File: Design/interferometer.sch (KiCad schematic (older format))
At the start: 30 parts, among them Q1 FDC637BNZ, U1 ADN8810ACPZ, U2 OPA320SAIDBVT, U3 ADR292GRUZ

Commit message: Modify schematic
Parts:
- added R? (x4): 100k, symbol R
- R3: value R -> 66.5R
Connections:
- net 3v3: now also R?.1, R?.1, R?.1, R?.1
- net ~CS: now also R?.2
- net ~SHDN: now also R?.2
- net ~laser_reset: now also R?.2
- net ~laser_standby: now also R?.2
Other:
- moved on the sheet: C10, C9, TP4
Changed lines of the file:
@@
 Text Label 6550 1700 0    60   ~ 0
 SCK
-Text Label 6550 2000 0    60   ~ 0
+Text Label 7050 2000 0    60   ~ 0
 ~CS
 Text Label 4050 2600 0    60   ~ 0
@@
 Text Label 6550 1600 0    60   ~ 0
 GND
-Text Label 2700 3600 1    60   ~ 0
+Text Label 2450 3900 1    60   ~ 0
 GND
 $Comp
 L GNDA #PWR01
 U 1 1 591C35DD
-P 2500 4050
-F 0 "#PWR01" H 2500 3800 50  0001 C CNN
-F 1 "GNDA" H 2505 3877 50  0000 C CNN
-F 2 "" H 2500 4050 50  0001 C CNN
-F 3 "" H 2500 4050 50  0001 C CNN
-	1    2500 4050
+P 2250 4350
+F 0 "#PWR01" H 2250 4100 50  0001 C CNN
+F 1 "GNDA" H 2255 4177 50  0000 C CNN
+F 2 "" H 2250 4350 50  0001 C CNN
+F 3 "" H 2250 4350 50  0001 C CNN
+	1    2250 4350
 	1    0    0    -1
 $EndComp
@@
 L Earth #PWR02
 U 1 1 591C415F
-P 2900 4050
-F 0 "#PWR02" H 2900 3800 50  0001 C CNN
-F 1 "Earth" H 2900 3900 50  0001 C CNN
-F 2 "" H 2900 4050 50  0001 C CNN
-F 3 "" H 2900 4050 50  0001 C CNN
-	1    2900 4050
+P 2650 4350
+F 0 "#PWR02" H 2650 4100 50  0001 C CNN
+F 1 "Earth" H 2650 4200 50  0001 C CNN
+F 2 "" H 2650 4350 50  0001 C CNN
+F 3 "" H 2650 4350 50  0001 C CNN
+	1    2650 4350
 	1    0    0    -1
 $EndComp
@@
 Text Label 7300 1450 0    60   ~ 0
 4.096_VREF
-Text Label 7450 1550 0    60   ~ 0
+Text Label 7400 1550 0    60   ~ 0
 ~laser_reset
-Text Label 8050 3000 0    60   ~ 0
+Text Label 8050 3000 2    60   ~ 0
 ~laser_standby
 NoConn ~ 10000 1400
@@
 L C C9
 U 1 1 591CDD86
-P 1050 5250
-F 0 "C9" H 1150 5250 50  0000 L CNN
-F 1 "22uF" H 1100 5150 50  0000 L CNN
-F 2 "" H 1088 5100 50  0001 C CNN
-F 3 "" H 1050 5250 50  0001 C CNN
-	1    1050 5250
+P 1050 5550
+F 0 "C9" H 1150 5550 50  0000 L CNN
+F 1 "22uF" H 1100 5450 50  0000 L CNN
+F 2 "" H 1088 5400 50  0001 C CNN
+F 3 "" H 1050 5550 50  0001 C CNN
+	1    1050 5550
 	1    0    0    -1
 $EndComp
@@
 L GNDA #PWR010
 U 1 1 591CE000
-P 1050 5500
-F 0 "#PWR010" H 1050 5250 50  0001 C CNN
-F 1 "GNDA" H 1055 5327 50  0000 C CNN
-F 2 "" H 1050 5500 50  0001 C CNN
-F 3 "" H 1050 5500 50  0001 C CNN
-	1    1050 5500
+P 1050 5800
+F 0 "#PWR010" H 1050 5550 50  0001 C CNN
+F 1 "GNDA" H 1055 5627 50  0000 C CNN
+F 2 "" H 1050 5800 50  0001 C CNN
+F 3 "" H 1050 5800 50  0001 C CNN
+	1    1050 5800
 	1    0    0    -1
 $EndComp
@@
 U 1 1 591CE293
 P 7230 4820
-F 0 "R3" H 7300 4866 50  0000 L CNN
-F 1 "R" H 7300 4775 50  0000 L CNN
+F 0 "R3" H 7000 4890 50  0000 L CNN
+F 1 "66.5R" H 6950 4790 50  0000 L CNN
 F 2 "Resistors_SMD:R_0805" V 7160 4820 50  0001 C CNN
 F 3 "" H 7230 4820 50  0001 C CNN
@@
 Text Label 5700 6300 2    60   ~ 0
 AVSS
-Text Label 800  5000 0    60   ~ 0
+Text Label 800  5300 0    60   ~ 0
 3v3
 $Comp
 L C C10
 U 1 1 591D633E
-P 2450 5250
-F 0 "C10" H 2550 5250 50  0000 L CNN
-F 1 "22uF" H 2500 5150 50  0000 L CNN
-F 2 "" H 2488 5100 50  0001 C CNN
-F 3 "" H 2450 5250 50  0001 C CNN
-	1    2450 5250
+P 2450 5550
+F 0 "C10" H 2550 5550 50  0000 L CNN
+F 1 "22uF" H 2500 5450 50  0000 L CNN
+F 2 "" H 2488 5400 50  0001 C CNN
+F 3 "" H 2450 5550 50  0001 C CNN
+	1    2450 5550
 	1    0    0    -1
 $EndComp
@@
 L GNDA #PWR011
 U 1 1 591D6345
-P 2450 5500
-F 0 "#PWR011" H 2450 5250 50  0001 C CNN
-F 1 "GNDA" H 2455 5327 50  0000 C CNN
-F 2 "" H 2450 5500 50  0001 C CNN
-F 3 "" H 2450 5500 50  0001 C CNN
-	1    2450 5500
-	1    0    0    -1
-$EndComp
-Text Label 2200 5000 0    60   ~ 0
+P 2450 5800
+F 0 "#PWR011" H 2450 5550 50  0001 C CNN
+F 1 "GNDA" H 2455 5627 50  0000 C CNN
+F 2 "" H 2450 5800 50  0001 C CNN
+F 3 "" H 2450 5800 50  0001 C CNN
+	1    2450 5800
+	1    0    0    -1
+$EndComp
+Text Label 2200 5300 0    60   ~ 0
 5v
 Text Label 10100 2600 0    60   ~ 0
@@
 	6200 1700 6550 1700
 Wire Wire Line
-	6200 2000 6550 2000
+	6200 2000 7050 2000
 Wire Wire Line
 	4300 2600 4050 2600
@@
 	475  4740 475  4735
 Wire Wire Line
-	2700 3600 2700 3900
-Wire Wire Line
-	2500 3900 2900 3900
-Wire Wire Line
-	2900 3900 2900 4050
-Wire Wire Line
-	2500 3900 2500 4050
-Connection ~ 2700 3900
+	2450 3900 2450 4200
+Wire Wire Line
+	2250 4200 2650 4200
+Wire Wire Line
+	2650 4200 2650 4350
+Wire Wire Line
+	2250 4200 2250 4350
+Connection ~ 2450 4200
 Wire Wire Line
 	9250 2700 9250 2850
@@
 	7300 1450 7900 1450
 Wire Wire Line
-	7900 1550 7450 1550
+	7400 1550 7900 1550
 Wire Wire Line
 	8750 2700 8750 3000
@@
 	7350 1850 7350 1750
 Wire Wire Line
-	800  5000 1050 5000
-Wire Wire Line
-	1050 5000 1050 5100
-Connection ~ 1050 5000
-Wire Wire Line
-	1050 5500 1050 5400
+	800  5300 1050 5300
+Wire Wire Line
+	1050 5300 1050 5400
+Connection ~ 1050 5300
+Wire Wire Line
+	1050 5800 1050 5700
 Wire Wire Line
 	7080 3645 7215 3645
@@
 	5750 6300 5700 6300
 Wire Wire Line
-	2200 5000 2450 5000
-Wire Wire Line
-	2450 5000 2450 5100
-Connection ~ 2450 5000
-Wire Wire Line
-	2450 5500 2450 5400
+	2200 5300 2450 5300
+Wire Wire Line
+	2450 5300 2450 5400
+Connection ~ 2450 5300
+Wire Wire Line
+	2450 5800 2450 5700
 Wire Wire Line
 	9000 750  9000 1000
@@
 	9250 2850 9500 2850
 Wire Wire Line
-	9200 4800 9550 4800
+	9200 4800 10750 4800
 Wire Wire Line
 	9500 4600 10000 4600
@@
 Wire Wire Line
 	8350 3900 8350 4000
-Text Label 9550 4800 2    60   ~ 0
+Text Label 10750 4800 0    60   ~ 0
 ~SHDN
 Wire Wire Line
@@
 	6110 6125 6000 6125
 Wire Wire Line
-	5970 5810 6320 5810
+	5970 5860 6320 5860
 $Comp
 L TESTPOINT TP4
 U 1 1 591DB78A
-P 6320 5810
-F 0 "TP4" H 6398 5934 40  0000 L CNN
-F 1 "TESTPOINT" H 6398 5866 30  0000 L CNN
-F 2 "Measurement_Points:Measurement_Point_Round-SMD-Pad_Big" H 6320 5810 60  0001 C CNN
-F 3 "" H 6320 5810 60  0000 C CNN
-	1    6320 5810
-	1    0    0    -1
-$EndComp
-Text Label 5970 5810 0    60   ~ 0
+P 6320 5860
+F 0 "TP4" H 6398 5984 40  0000 L CNN
+F 1 "TESTPOINT" H 6398 5916 30  0000 L CNN
+F 2 "Measurement_Points:Measurement_Point_Round-SMD-Pad_Big" H 6320 5860 60  0001 C CNN
+F 3 "" H 6320 5860 60  0000 C CNN
+	1    6320 5860
+	1    0    0    -1
+$EndComp
+Text Label 5970 5860 0    60   ~ 0
 3v3
 Wire Notes Line
@@
 NoConn ~ 6120 3815
 NoConn ~ 7080 3815
+$Comp
+L R R?
+U 1 1 591DD952
+P 10550 4550
+F 0 "R?" H 10620 4596 50  0000 L CNN
+F 1 "100k" H 10620 4505 50  0000 L CNN
+F 2 "" V 10480 4550 50  0001 C CNN
+F 3 "" H 10550 4550 50  0001 C CNN
+	1    10550 4550
+	1    0    0    -1
+$EndComp
+Connection ~ 10550 4800
+Wire Wire Line
+	10550 4700 10550 4800
+Wire Wire Line
+	10550 4400 10550 4300
+Wire Wire Line
+	10550 4300 10700 4300
+Text Label 10700 4300 0    60   ~ 0
+3v3
+$Comp
+L R R?
+U 1 1 591DE4AD
+P 8200 2750
+F 0 "R?" H 8270 2796 50  0000 L CNN
+F 1 "100k" H 8270 2705 50  0000 L CNN
+F 2 "" V 8130 2750 50  0001 C CNN
+F 3 "" H 8200 2750 50  0001 C CNN
+	1    8200 2750
+	1    0    0    -1
+$EndComp
+Wire Wire Line
+	8200 2900 8200 3000
+Connection ~ 8200 3000
+Wire Wire Line
+	8200 2600 8000 2600
+Text Label 8000 2600 0    60   ~ 0
+3v3
+$Comp
+L R R?
+U 1 1 591DEC98
+P 6900 1800
+F 0 "R?" H 6970 1846 50  0000 L CNN
+F 1 "100k" H 6970 1755 50  0000 L CNN
+F 2 "" V 6830 1800 50  0001 C CNN
+F 3 "" H 6900 1800 50  0001 C CNN
+	1    6900 1800
+	1    0    0    -1
+$EndComp
+Wire Wire Line
+	6900 1950 6900 2000
+Connection ~ 6900 2000
+Wire Wire Line
+	6900 1650 6900 1550
+Wire Wire Line
+	6900 1550 7100 1550
+Text Label 7100 1550 2    60   ~ 0
+3v3
+$Comp
+L R R?
+U 1 1 591DF4B3
+P 7450 1200
+F 0 "R?" H 7520 1246 50  0000 L CNN
+F 1 "100k" H 7520 1155 50  0000 L CNN
+F 2 "" V 7380 1200 50  0001 C CNN
+F 3 "" H 7450 1200 50  0001 C CNN
+	1    7450 1200
+	1    0    0    -1
+$EndComp
+Wire Wire Line
+	7450 1050 7450 1000
+Wire Wire Line
+	7450 1000 7650 1000
+Text Label 7650 1000 2    60   ~ 0
+3v3
+Wire Wire Line
+	7450 1550 7450 1350
+Connection ~ 7450 1550
 $EndSCHEMATC

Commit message: Modify schematic
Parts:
- added D1, D2: LED, LEDs:LED_0805, symbol LED
- added JP5: Jumper_NC_Dual, freetronics_footprints:1X03, symbol Jumper_NC_Dual
- added R10: 100R, Resistors_SMD:R_0805_HandSoldering, symbol R
- added R9: 220R, Resistors_SMD:R_0805_HandSoldering, symbol R
- C10, C8, C9: footprint (none) -> Capacitors_SMD:C_1210_HandSoldering
- LD1: footprint (none) -> ADN8810ACPZ:ADL-65055TL
- R5: renamed from R?; footprint (none) -> Resistors_SMD:R_0805_HandSoldering; manf# (none) -> ERA-6AEB104V
- R6, R7, R8: renamed from R?; footprint (none) -> Resistors_SMD:R_0805_HandSoldering
- U3: manf# (none) -> ADR292GRUZ
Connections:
- net 3v3: now also D2.2 (A)
- net 5v: now also D1.2 (A)
- net A0: now also JP5.3; no longer C12.1, R4.1, U2.1 (VOUT)
- net AVSS: no longer C1.2, C11.2, C3.2, C7.1, R1.1
- net Earth: now also C1.2, C11.2, C3.2, C7.1, R1.1, R10.2, R9.2
- net A1: no longer names the net of SHIELD1.AD1
- net A2: no longer names the net of SHIELD1.AD2
- net A3: no longer names the net of SHIELD1.AD3
- net A4: no longer names the net of SHIELD1.AD4
- net A5: no longer names the net of SHIELD1.AD5
- new net: C12.1, JP5.2, R4.1, U2.1 (VOUT)
- new net: D1.1 (K), R9.1
- new net: D2.1 (K), R10.1
- new net scope_probe: JP5.1
- no-connect marks 31 -> 37

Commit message: Modify design
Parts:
- added C13, C14: 0.1uF, Capacitors_SMD:C_0805_HandSoldering, symbol C
- added R11: 5.1k, Resistors_SMD:R_0805_HandSoldering, symbol R
- TP1, TP2, TP3, TP4: footprint Measurement_Points:Measurement_Point_Round-SMD-Pad_Big -> Measurement_Points:Measurement_Point_Round-SMD-Pad_Small
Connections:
- net AVSS: now also R1.1, C13.1; no longer C5.2
- net Earth: now also C5.2, C13.2, R11.2; no longer R1.1
- net at C12.1, R4.1, U2.1 (VOUT): now also C14.2; no longer JP5.2
- new net: C14.1, JP5.2, R11.1
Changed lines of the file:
@@
 F 0 "TP2" H 7208 5854 40  0000 L CNN
 F 1 "TESTPOINT" H 7208 5786 30  0000 L CNN
-F 2 "Measurement_Points:Measurement_Point_Round-SMD-Pad_Big" H 7130 5730 60  0001 C CNN
+F 2 "Measurement_Points:Measurement_Point_Round-SMD-Pad_Small" H 7130 5730 60  0001 C CNN
 F 3 "" H 7130 5730 60  0000 C CNN
 	1    7130 5730
@@
 F 0 "TP3" H 5955 6275 40  0000 L CNN
 F 1 "TESTPOINT" H 5830 6210 30  0000 L CNN
-F 2 "Measurement_Points:Measurement_Point_Round-SMD-Pad_Big" H 6110 6205 60  0001 C CNN
+F 2 "Measurement_Points:Measurement_Point_Round-SMD-Pad_Small" H 6110 6205 60  0001 C CNN
 F 3 "" H 6110 6205 60  0000 C CNN
 	1    6110 6205
@@
 	1    0    0    -1
 $EndComp
-Text Label 1200 2000 0    60   ~ 0
-AVSS
 Text Label 6905 5080 0    60   ~ 0
 AVSS
@@
 U 1 1 591DD2E2
 P 9200 4600
-F 0 "U2" H 9250 4750 50  0000 L CNN
-F 1 "OPA320SAIDBVT" H 9250 4850 50  0000 L CNN
+F 0 "U2" H 9100 4800 50  0000 L CNN
+F 1 "OPA320SAIDBVT" H 9100 4900 50  0000 L CNN
 F 2 "TO_SOT_Packages_SMD:SOT-23-6" H 9400 4050 50  0001 C CNN
 F 3 "" H 9200 4600 50  0001 C CNN
@@
 F 0 "TP4" H 6398 5984 40  0000 L CNN
 F 1 "TESTPOINT" H 6398 5916 30  0000 L CNN
-F 2 "Measurement_Points:Measurement_Point_Round-SMD-Pad_Big" H 6320 5860 60  0001 C CNN
+F 2 "Measurement_Points:Measurement_Point_Round-SMD-Pad_Small" H 6320 5860 60  0001 C CNN
 F 3 "" H 6320 5860 60  0000 C CNN
 	1    6320 5860
@@
 	1450 1365 1450 1550
 Wire Wire Line
-	1450 1850 1450 2000
-Wire Wire Line
-	1450 2000 1200 2000
+	1450 1850 1450 2150
 Wire Wire Line
 	7230 5080 6905 5080
@@
 	9200 4800 10750 4800
 Wire Wire Line
-	9500 4600 10100 4600
-Wire Wire Line
 	9100 4900 9100 5000
 Wire Wire Line
-	9100 5000 9200 5000
+	8500 5000 9200 5000
 Wire Wire Line
 	9100 4000 9100 4300
@@
 Connection ~ 8650 4000
 Wire Wire Line
-	8350 3600 8350 3500
-Wire Wire Line
-	8350 3500 9050 3500
-Wire Wire Line
 	8650 3500 8650 3600
 Connection ~ 8650 3500
@@
 Wire Wire Line
 	3650 2850 3650 2800
-Wire Wire Line
-	10100 4600 10100 4200
 Text Label 5975 5575 0    60   ~ 0
 A0
@@
 F 0 "TP1" H 6183 5619 40  0000 L CNN
 F 1 "TESTPOINT" H 6183 5551 30  0000 L CNN
-F 2 "Measurement_Points:Measurement_Point_Round-SMD-Pad_Big" H 6105 5495 60  0001 C CNN
+F 2 "Measurement_Points:Measurement_Point_Round-SMD-Pad_Small" H 6105 5495 60  0001 C CNN
 F 3 "" H 6105 5495 60  0000 C CNN
 	1    6105 5495
@@
 $Comp
 L GNDA #PWR015
-U 1 1 591F395F
-P 9050 3500
-F 0 "#PWR015" H 9050 3250 50  0001 C CNN
-F 1 "GNDA" H 9055 3327 50  0000 C CNN
-F 2 "" H 9050 3500 50  0001 C CNN
-F 3 "" H 9050 3500 50  0001 C CNN
-	1    9050 3500
-	1    0    0    -1
-$EndComp
-$Comp
-L GNDA #PWR016
 U 1 1 591F4592
 P 10200 1350
-F 0 "#PWR016" H 10200 1100 50  0001 C CNN
+F 0 "#PWR015" H 10200 1100 50  0001 C CNN
 F 1 "GNDA" H 10350 1250 50  0000 C CNN
 F 2 "" H 10200 1350 50  0001 C CNN
@@
 	8750 1100 8750 1000
 $Comp
-L GNDA #PWR017
+L GNDA #PWR016
 U 1 1 591F4F47
 P 8750 1100
-F 0 "#PWR017" H 8750 850 50  0001 C CNN
+F 0 "#PWR016" H 8750 850 50  0001 C CNN
 F 1 "GNDA" V 8850 1150 50  0000 C CNN
 F 2 "" H 8750 1100 50  0001 C CNN
@@
 $EndComp
 $Comp
-L GNDA #PWR018
+L GNDA #PWR017
 U 1 1 591F5F82
 P 3405 5790
-F 0 "#PWR018" H 3405 5540 50  0001 C CNN
+F 0 "#PWR017" H 3405 5540 50  0001 C CNN
 F 1 "GNDA" H 3410 5617 50  0000 C CNN
 F 2 "" H 3405 5790 50  0001 C CNN
@@
 Wire Wire Line
 	3405 5790 3405 5680
+$Comp
+L C C13
+U 1 1 592057BF
+P 8500 5150
+F 0 "C13" H 8200 5200 50  0000 L CNN
+F 1 "0.1uF" H 8150 5100 50  0000 L CNN
+F 2 "Capacitors_SMD:C_0805_HandSoldering" H 8538 5000 50  0001 C CNN
+F 3 "" H 8500 5150 50  0001 C CNN
+	1    8500 5150
+	1    0    0    -1
+$EndComp
+Connection ~ 9100 5000
+$Comp
+L GNDA #PWR018
+U 1 1 59205C76
+P 8500 5350
+F 0 "#PWR018" H 8500 5100 50  0001 C CNN
+F 1 "GNDA" H 8505 5177 50  0000 C CNN
+F 2 "" H 8500 5350 50  0001 C CNN
+F 3 "" H 8500 5350 50  0001 C CNN
+	1    8500 5350
+	1    0    0    -1
+$EndComp
+Wire Wire Line
+	8500 5350 8500 5300
+Wire Wire Line
+	9050 3500 8650 3500
+Text Label 9050 3500 0    60   ~ 0
+AVSS
+Wire Wire Line
+	8350 3600 8350 3500
+Wire Wire Line
+	8350 3500 7850 3500
+Wire Wire Line
+	7850 3500 7850 3650
+$Comp
+L GNDA #PWR019
+U 1 1 59206D7C
+P 7850 3650
+F 0 "#PWR019" H 7850 3400 50  0001 C CNN
+F 1 "GNDA" H 7650 3550 50  0000 C CNN
+F 2 "" H 7850 3650 50  0001 C CNN
+F 3 "" H 7850 3650 50  0001 C CNN
+	1    7850 3650
+	1    0    0    -1
+$EndComp
+$Comp
+L GNDA #PWR020
+U 1 1 5920C7C9
+P 1450 2150
+F 0 "#PWR020" H 1450 1900 50  0001 C CNN
+F 1 "GNDA" H 1455 1977 50  0000 C CNN
+F 2 "" H 1450 2150 50  0001 C CNN
+F 3 "" H 1450 2150 50  0001 C CNN
+	1    1450 2150
+	1    0    0    -1
+$EndComp
+Wire Wire Line
+	9500 4600 9750 4600
+$Comp
+L R R11
+U 1 1 592166B5
+P 10100 5050
+F 0 "R11" H 10170 5096 50  0000 L CNN
+F 1 "5.1k" H 10170 5005 50  0000 L CNN
+F 2 "Resistors_SMD:R_0805_HandSoldering" V 10030 5050 50  0001 C CNN
+F 3 "" H 10100 5050 50  0001 C CNN
+	1    10100 5050
+	1    0    0    -1
+$EndComp
+$Comp
+L C C14
+U 1 1 592167F4
+P 9900 4600
+F 0 "C14" V 9648 4600 50  0000 C CNN
+F 1 "0.1uF" V 9739 4600 50  0000 C CNN
+F 2 "Capacitors_SMD:C_0805_HandSoldering" H 9938 4450 50  0001 C CNN
+F 3 "" H 9900 4600 50  0001 C CNN
+	1    9900 4600
+	0    1    1    0
+$EndComp
+Wire Wire Line
+	10050 4600 10100 4600
+Wire Wire Line
+	10100 4200 10100 4900
+Connection ~ 10100 4600
+$Comp
+L GNDA #PWR021
+U 1 1 59216D38
+P 10100 5300
+F 0 "#PWR021" H 10100 5050 50  0001 C CNN
+F 1 "GNDA" H 10105 5127 50  0000 C CNN
+F 2 "" H 10100 5300 50  0001 C CNN
+F 3 "" H 10100 5300 50  0001 C CNN
+	1    10100 5300
+	1    0    0    -1
+$EndComp
+Wire Wire Line
+	10100 5300 10100 5200
 $EndSCHEMATC

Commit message: finalise layout
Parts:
- added J1: GS2, Connectors:GS2, symbol GS2
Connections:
- net AVSS: now also J1.1 (G1)
- net Earth: now also J1.2 (G2)
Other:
- note added: "Alternate tie point"
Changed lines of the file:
@@
 U 1 1 591ECA9B
 P 10100 4100
-F 0 "JP5" H 10250 4615 50  0000 L CNN
-F 1 "Jumper_NC_Dual" H 9800 4515 50  0000 L CNN
+F 0 "JP5" H 9765 4325 50  0000 L CNN
+F 1 "Jumper_NC_Dual" H 9760 4250 50  0000 L CNN
 F 2 "freetronics_footprints:1X03" H 10100 4100 50  0001 C CNN
 F 3 "" H 10100 4100 50  0001 C CNN
@@
 Wire Wire Line
 	10100 5300 10100 5200
+$Comp
+L GS2 J1
+U 1 1 59219F5F
+P 1750 6900
+F 0 "J1" V 1545 6900 50  0000 C CNN
+F 1 "GS2" V 1636 6900 50  0000 C CNN
+F 2 "Connectors:GS2" V 1824 6900 50  0001 C CNN
+F 3 "" H 1750 6900 50  0001 C CNN
+	1    1750 6900
+	0    1    1    0
+$EndComp
+$Comp
+L GNDA #PWR022
+U 1 1 5921A1DD
+P 1550 7050
+F 0 "#PWR022" H 1550 6800 50  0001 C CNN
+F 1 "GNDA" H 1555 6877 50  0000 C CNN
+F 2 "" H 1550 7050 50  0001 C CNN
+F 3 "" H 1550 7050 50  0001 C CNN
+	1    1550 7050
+	1    0    0    -1
+$EndComp
+Wire Wire Line
+	1550 7050 1550 6900
+Text Label 2100 6900 0    60   ~ 0
+AVSS
+Wire Wire Line
+	1950 6900 2100 6900
+Wire Notes Line
+	3040 6540 3040 7795
+Text Notes 3035 7795 2    60   ~ 0
+Alternate tie point
 $EndSCHEMATC

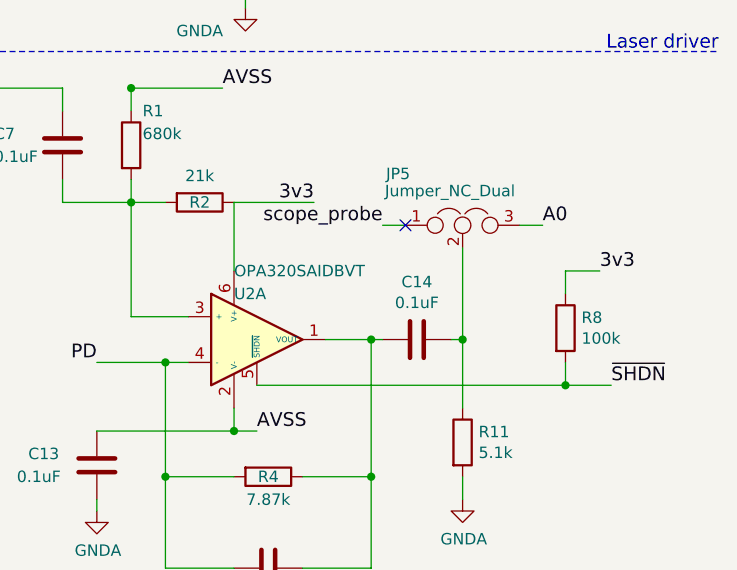
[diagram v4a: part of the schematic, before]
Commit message: modify design for manufacturing
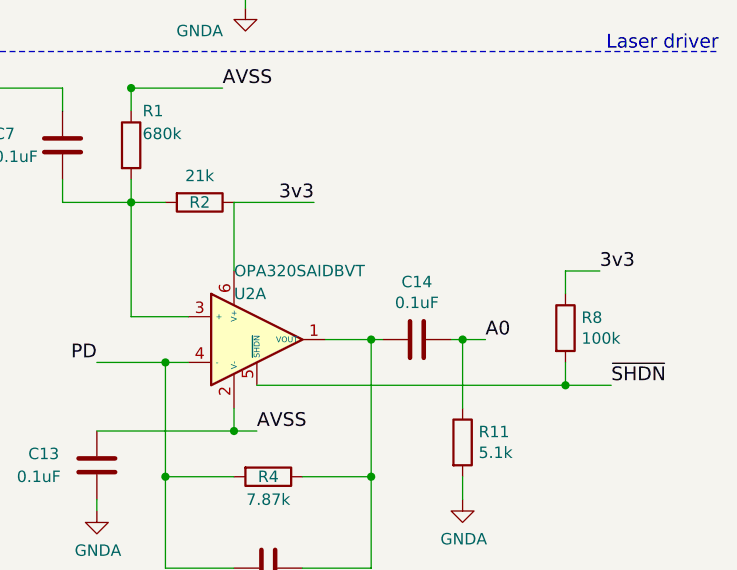
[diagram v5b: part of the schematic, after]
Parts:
- removed JP5: Jumper_NC_Dual, freetronics_footprints:1X03, symbol Jumper_NC_Dual
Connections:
- net A0: now also C14.1, R11.1
- no-connect marks 37 -> 36
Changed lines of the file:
@@
-	1    0    0    -1
-$EndComp
-$Comp
-L Jumper_NC_Dual JP5
-U 1 1 591ECA9B
-P 10100 4100
-F 0 "JP5" H 9765 4325 50  0000 L CNN
-F 1 "Jumper_NC_Dual" H 9760 4250 50  0000 L CNN
-F 2 "freetronics_footprints:1X03" H 10100 4100 50  0001 C CNN
-F 3 "" H 10100 4100 50  0001 C CNN
-	1    10100 4100
 	1    0    0    -1
 $EndComp
@@
 	1    0    0    -1
 $EndComp
-Wire Wire Line
-	9850 4100 9750 4100
-Text Label 9750 4100 2    60   ~ 0
-scope_probe
-Wire Wire Line
-	10350 4100 10450 4100
-Text Label 10450 4100 0    60   ~ 0
+Text Label 10200 4600 0    60   ~ 0
 A0
-NoConn ~ 9850 4100
 $Comp
 L GNDA #PWR015
@@
 $EndComp
 Wire Wire Line
-	10050 4600 10100 4600
-Wire Wire Line
-	10100 4200 10100 4900
-Connection ~ 10100 4600
+	10050 4600 10200 4600
 $Comp
 L GNDA #PWR021
@@
 Text Notes 3035 7795 2    60   ~ 0
 Alternate tie point
+Wire Wire Line
+	10100 4900 10100 4600
+Connection ~ 10100 4600
 $EndSCHEMATC

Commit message: Cleanup
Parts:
- C1, C10, C11, C12, C13, C14, C2, C3, C4, C5, C6, C7, C8, C9: symbol C -> Device:C
- D1, D2: symbol LED -> Device:LED
- J1: symbol GS2 -> interferometer-rescue:GS2
- JP1, JP2, JP3, JP4: symbol Jumper_NC_Dual -> Device:Jumper_NC_Dual
- LD1: symbol Laserdiode_N_TYPE -> Device:Laserdiode_N_TYPE
- Q1: symbol FDC637BNZ -> ADN8810ACPZ:FDC637BNZ
- R1, R10, R11, R2, R3, R4, R5, R6, R7, R8, R9: symbol R -> Device:R
- SHIELD1: symbol ARDUINO_SHIELD -> freetronics_schematic:ARDUINO_SHIELD
- TP1, TP2, TP3, TP4: symbol TESTPOINT -> freetronics_schematic:TESTPOINT
- U1: symbol ADN8810ACP -> ADN8810ACPZ:ADN8810ACP
- U2: symbol OPA320SAIDBVT -> ADN8810ACPZ:OPA320SAIDBVT
- U3: symbol ADR292GRUZ -> ADN8810ACPZ:ADR292GRUZ
